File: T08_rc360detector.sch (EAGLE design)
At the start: 46 parts, among them IC2 LM317MSTT3, U1 ATmega328, X1 SSW-101-02-S-D, X2 332-04, X4 87758-0616, X5 87758-0616

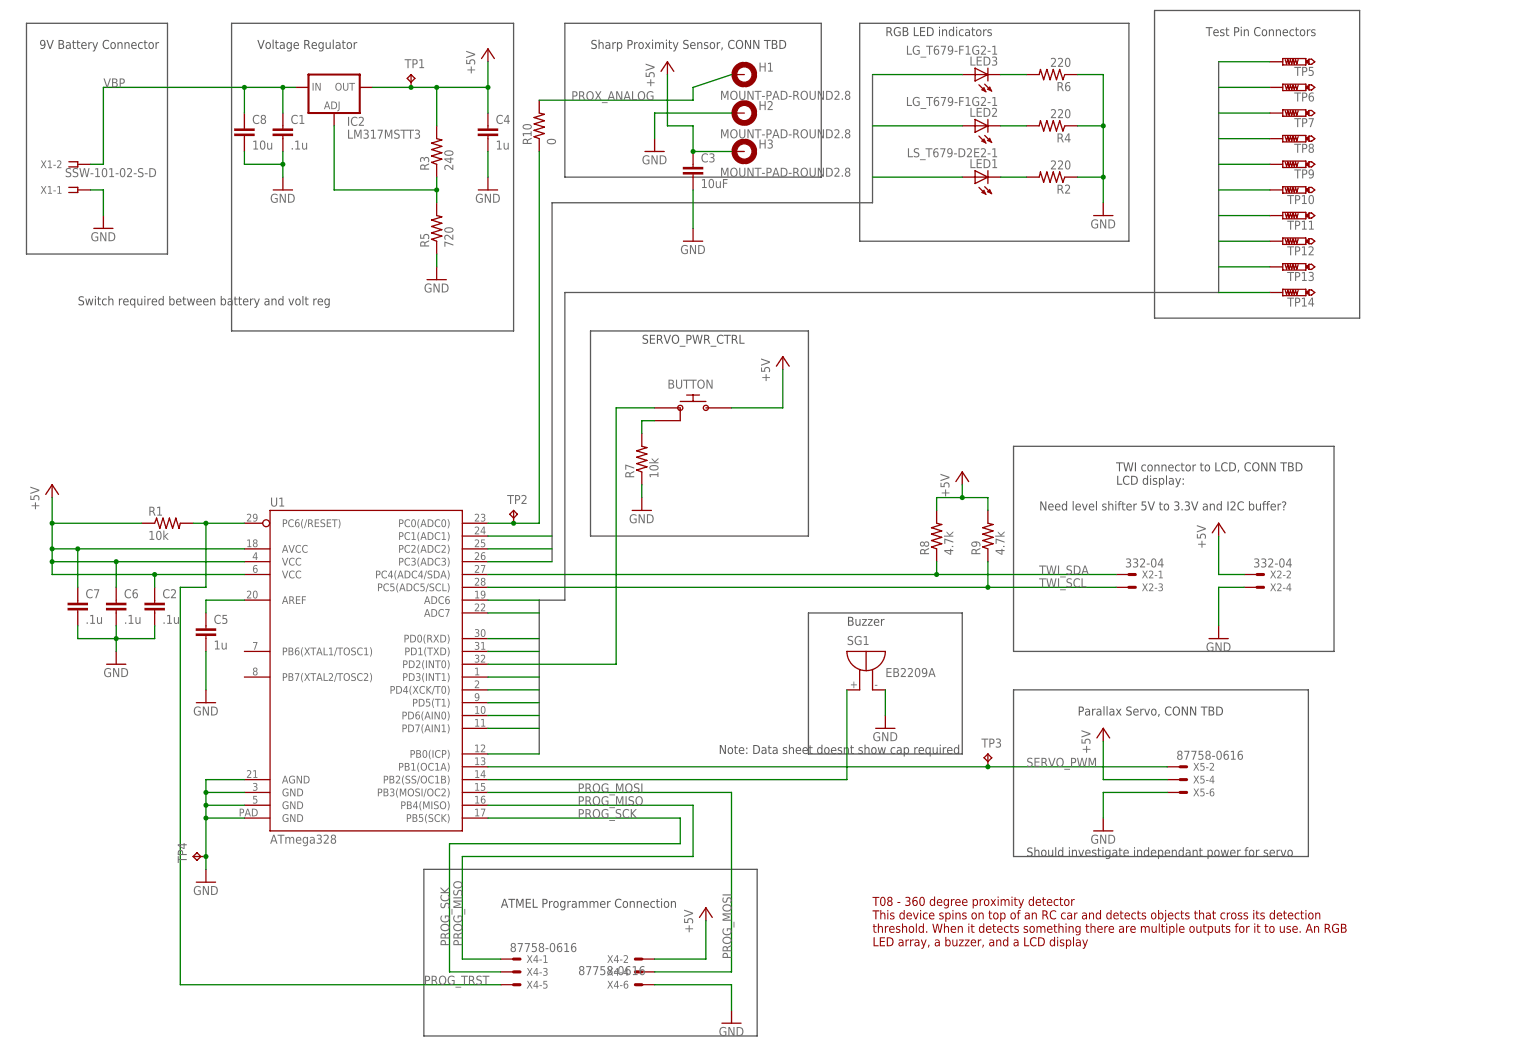
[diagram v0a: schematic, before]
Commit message: First pass at board layout
Started board layout. The problems:
-The current atmega328 block is way too small for us to solder, changed
to the pdip for the moment
-not sure if I got the rules check file working
-PCB layers are at 16, and it should be 2
-Need mounting screws tied to ground added to sch
-Added second power supply for servo
-Need to change layout to buzzer I found. Dimensions in components wiki
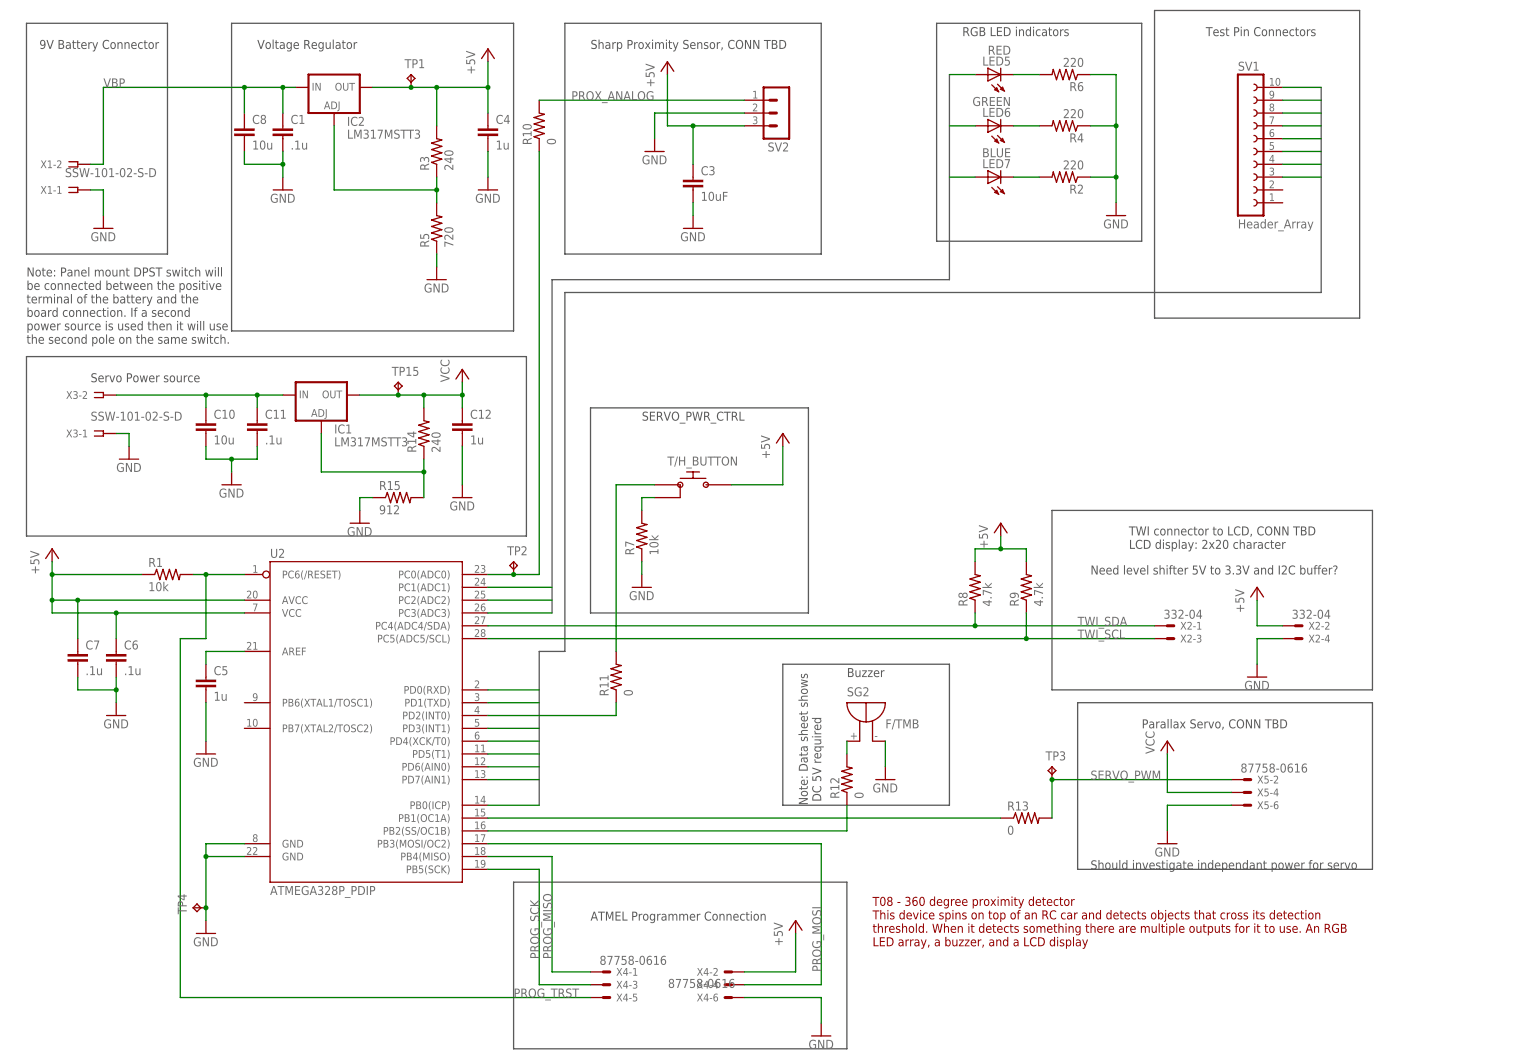
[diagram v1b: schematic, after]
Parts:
- removed BUTTON: PR141C, 360prox:PR141C
- removed C2: .1u, rcl:C-EUC0805
- removed H1, H2, H3: MOUNT-PAD-ROUND2.8, holes:MOUNT-PAD-ROUND2.8
- removed LED1: LS_T679-D2E2-1, led:LS_T679-D2E2-1
- removed LED2, LED3: LG_T679-F1G2-1, led:LG_T679-F1G2-1
- removed SG1: EB2209A, buzzer:EB2209A
- removed TP10, TP11, TP12, TP13, TP14, TP5, TP6, TP7, TP8, TP9: PTR1PAD1-20, testpad:PTR1PAD1-20
- removed U1: ATmega328, SparkFun-DigitalIC:ATMEGA328P_MLFMLF32
- added C10: 10u, rcl:C-EUC0805
- added C11: .1u, resistor:C-EUC0805
- added C12: 1u, resistor:C-EUC0805
- added IC1: LM317MSTT3, v-reg:LM317MSTT3
- added LED5: RED, led:LEDLD260
- added LED6: GREEN, led:LEDLD260
- added LED7: BLUE, led:LEDLD260
- added R11, R12, R13: 0, rcl:R-US_R0805
- added R14: 240, rcl:R-US_R0805
- added R15: 912, rcl:R-US_R0805
- added SG2: F/TMB, buzzer:F/TMB
- added SV1: Header_Array, con-lsta:FE10-1
- added SV2: (no value), con-lstb:MA03-1
- added T/H_BUTTON: PR141C, 360prox:PR141C
- added TP15: TPTP15R, testpad:TPTP15R
- added U2: ATMEGA328P_PDIP, SparkFun-DigitalIC:ATMEGA328P_PDIP
- added X3: SSW-101-02-S-D, con-samtec:SSW-101-02-S-D
- C1, C4, C5: device rcl:C-EUC0603 -> resistor:C-EUC0805
- R1, R3, R5: device rcl:R-US_R0603 -> rcl:R-US_R0805
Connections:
- removed net TP0: TP5.TP, U1.ADC6
- removed net TP1: TP6.TP, U1.ADC7
- new net N$10: R12.1, U2.PB2(SS/OC1B)
- new net N$11: R13.1, U2.PB1(OC1A)
- new net N$13: IC1.ADJ, R14.1, R15.2
- new net N$14: C10.1, C11.1, IC1.IN, X3-2.1
- new net N$6: R11.2, T/H_BUTTON.IN
- new net VCC: C12.1, IC1.OUT, R14.2, TP15.TP, X5-4.S
- net +5V: now also SV2.3, T/H_BUTTON.OUT, U2.AVCC, U2.VCC; no longer BUTTON.OUT, C2.1, H3.MOUNT, U1.AVCC, U1.VCC@4, U1.VCC@6, X5-4.S
- net AREF: now also U2.AREF; no longer U1.AREF
- net GND: now also C10.2, C11.2, C12.2, R15.1, SG2.-, SV2.2, U2.GND@1, U2.GND@2, X3-1.1; no longer C2.2, H2.MOUNT, SG1.-, U1.AGND, U1.GND@3, U1.GND@5, U1.GND@PAD
- net LED0: now also LED5.A, U2.PC1(ADC1); no longer LED1.A, U1.PC1(ADC1)
- net LED1: now also LED6.A, U2.PC2(ADC2); no longer LED2.A, U1.PC2(ADC2)
- net LED2: now also LED7.A, U2.PC3(ADC3); no longer LED3.A, U1.PC3(ADC3)
- net N$1: now also T/H_BUTTON.GND; no longer BUTTON.GND
- net N$3: now also R11.1, U2.PD2(INT0); no longer BUTTON.IN, U1.PD2(INT0)
- net N$4: now also R12.2, SG2.+; no longer SG1.+, U1.PB2(SS/OC1B)
- net N$5: now also LED5.C; no longer LED3.C
- net N$7: now also LED6.C; no longer LED2.C
- net N$8: now also LED7.C; no longer LED1.C
- net N$9: now also U2.PC0(ADC0); no longer U1.PC0(ADC0)
- net PROG_MISO: now also U2.PB4(MISO); no longer U1.PB4(MISO)
- net PROG_MOSI: now also U2.PB3(MOSI/OC2); no longer U1.PB3(MOSI/OC2)
- net PROG_SCK: now also U2.PB5(SCK); no longer U1.PB5(SCK)
- net PROG_TRST: now also U2.PC6(/RESET); no longer U1.PC6(/RESET)
- net PROX_ANALOG: now also SV2.1; no longer H1.MOUNT
- net SERVO_PWM: now also R13.2; no longer U1.PB1(OC1A)
- net TP2: now also SV1.3, U2.PD0(RXD); no longer TP7.TP, U1.PD0(RXD)
- net TP3: now also SV1.4, U2.PD1(TXD); no longer TP8.TP, U1.PD1(TXD)
- net TP4: now also SV1.5, U2.PD3(INT1); no longer TP9.TP, U1.PD3(INT1)
- net TP5: now also SV1.6, U2.PD4(XCK/T0); no longer TP10.TP, U1.PD4(XCK/T0)
- net TP6: now also SV1.7, U2.PD5(T1); no longer TP11.TP, U1.PD5(T1)
- net TP7: now also SV1.8, U2.PD6(AIN0); no longer TP12.TP, U1.PD6(AIN0)
- net TP8: now also SV1.9, U2.PD7(AIN1); no longer TP13.TP, U1.PD7(AIN1)
- net TP9: now also SV1.10, U2.PB0(ICP); no longer TP14.TP, U1.PB0(ICP)
- net TWI_SCL: now also U2.PC5(ADC5/SCL); no longer U1.PC5(ADC5/SCL)
- net TWI_SDA: now also U2.PC4(ADC4/SDA); no longer U1.PC4(ADC4/SDA)
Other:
- note added: "Note: Data sheet shows DC 5V required"
- note added: "Note: Panel mount DPST switch will be connected between the positive terminal of the battery and the board connection. If a second power source is used then it will use the second pole on the same switch."
- note added: "Servo Power source"
- note added: "TWI connector to LCD, CONN TBD LCD display: 2x20 character"
- note removed: "Note: Data sheet doesnt show cap required"
- note removed: "Switch required between battery and volt reg"
- note removed: "TWI connector to LCD, CONN TBD LCD display:"
- moved on the sheet: C3, C5, C6, C7, R1, R2, R4, R6, R7, R8, R9, TP2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

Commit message: 2nd pass
-Added custom library that contains button and buzzer
-Routed rest of connections. Left TWI interface out until Jared adds the
finished connections to the schematic
-Added screw holes, can resize if we want bigger screws
-Added some basic silk screen
-Added jumper for servo so we can switch it between if needed.
-Still need to find actual LEDs, until then there are generic T/H
-Havnt touched DRC, must look into in future
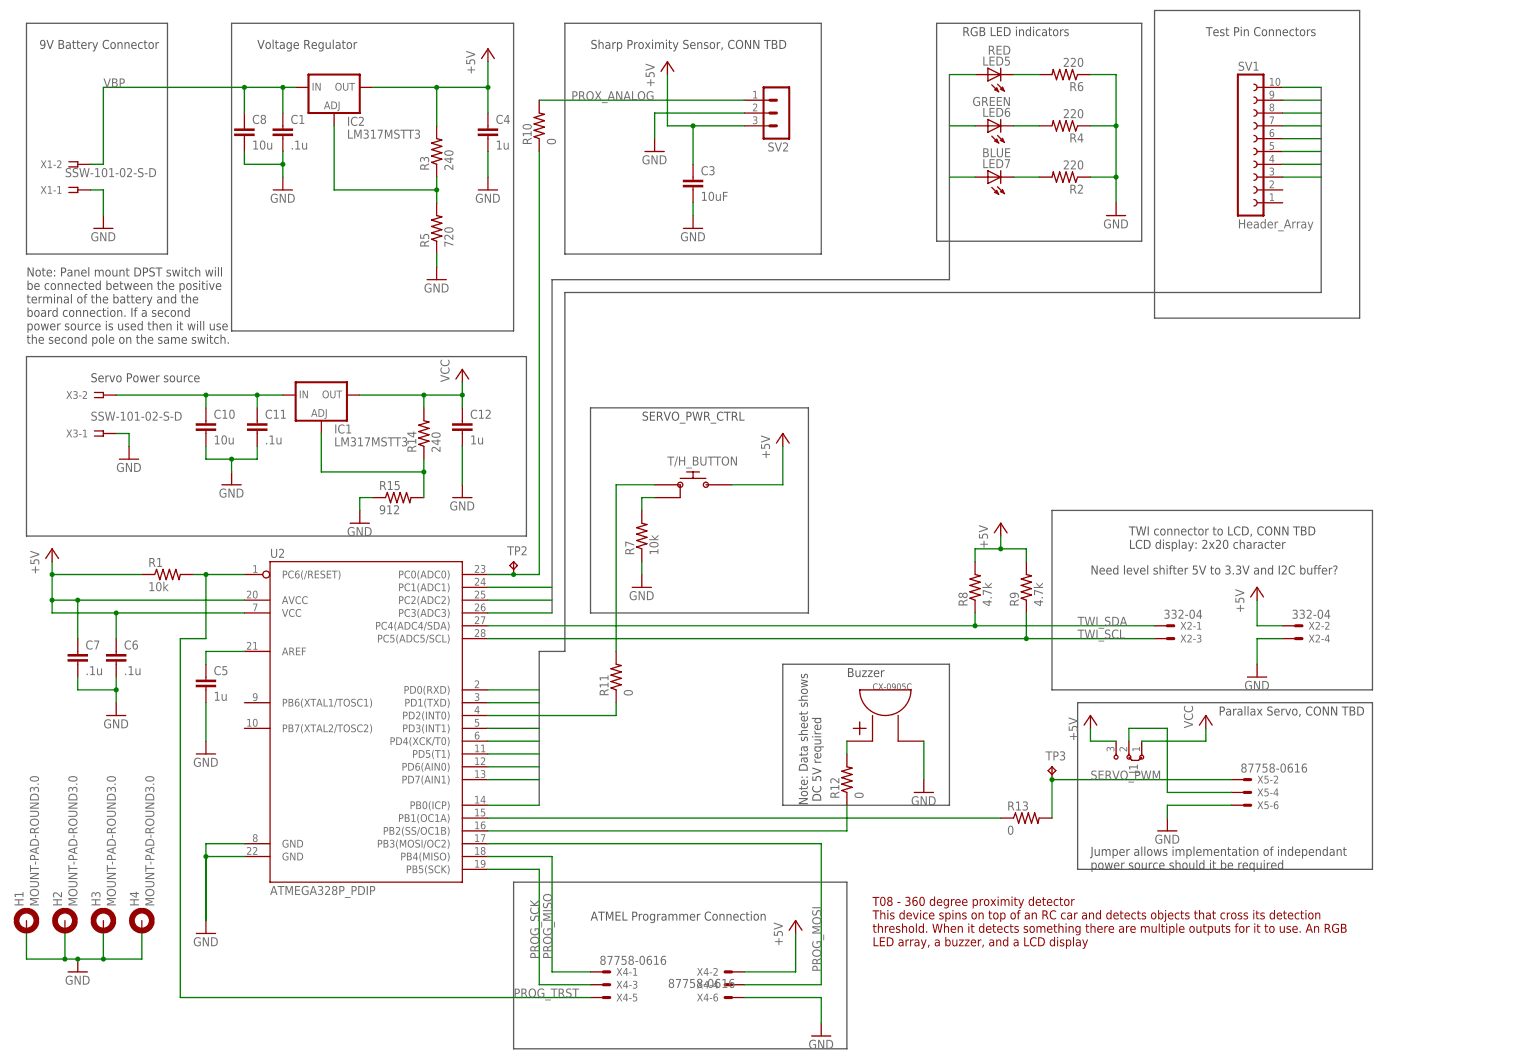
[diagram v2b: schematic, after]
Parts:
- removed SG2: F/TMB, buzzer:F/TMB
- removed TP1, TP4: TPPAD1-17, testpad:TPPAD1-17
- removed TP15: TPTP15R, testpad:TPTP15R
- added CX-0905C: CX-0905C, 360prox:CX-0905C
- added H1, H2, H3, H4: MOUNT-PAD-ROUND3.0, holes:MOUNT-PAD-ROUND3.0
- added J1: (no value), jumper:J2X2MM
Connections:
- new net N$16: J1.2, X5-4.S
- net +5V: now also J1.3; no longer TP1.TP
- net GND: now also CX-0905C.OUT, H1.MOUNT, H2.MOUNT, H3.MOUNT, H4.MOUNT; no longer SG2.-, TP4.TP
- net N$4: now also CX-0905C.IN; no longer SG2.+
- net VCC: now also J1.1; no longer TP15.TP, X5-4.S
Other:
- note added: "Jumper allows implementation of independant power source should it be required"
- note removed: "Should investigate independant power for servo"

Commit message: Update
Rerouted layout with new TWI circuitry. The logic converter IC is so
small the chip doesnt pass DRC, so I informed Jared and he's looking
into an alternate solution. Also the current chip is PDIP but I'm
debating changing it to TQFP. Will need to discuss tomorrow.
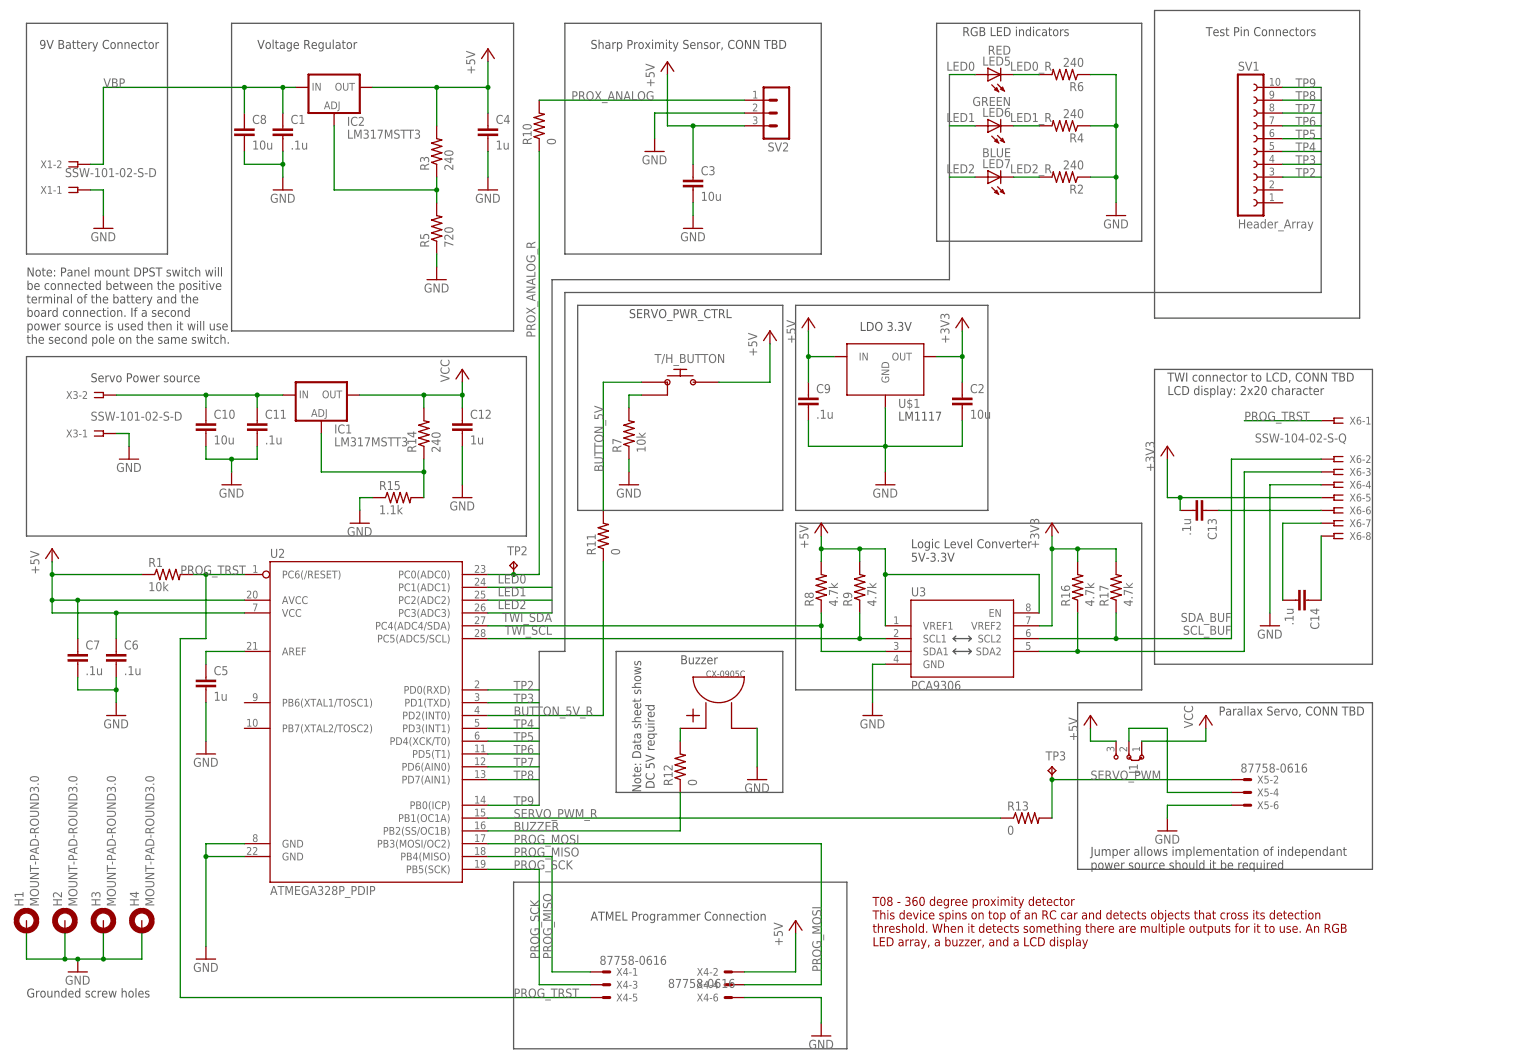
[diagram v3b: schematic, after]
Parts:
- removed X2: 332-04, con-garry:332-04
- added C13, C14, C9: .1u, resistor:C-EUC0805
- added C2: 10u, rcl:C-EUC0805
- added R16, R17: 4.7k, rcl:R-US_R0805
- added U$1: LM1117, 360prox:LM1117
- added U3: PCA9306, SparkFun-DigitalIC:PCA9306
- added X6: SSW-104-02-S-Q, con-samtec:SSW-104-02-S-Q
- C3: value 10uF -> 10u
- R15: value 912 -> 1.1k
- R2, R4, R6: value 220 -> 240
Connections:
- net N$10 renamed BUZZER
- net N$11 renamed SERVO_PWM_R
- net N$3 renamed BUTTON_5V_R
- net N$5 renamed LED0_R
- net N$6 renamed BUTTON_5V
- net N$7 renamed LED1_R
- net N$8 renamed LED2_R
- net N$9 renamed PROX_ANALOG_R
- new net +3V3: C13.2, C2.1, R16.2, R17.2, U$1.OUT, U3.VREF2, X6-5.1
- new net N$18: C13.1, X6-6.1
- new net N$19: C14.2, X6-7.1
- new net N$20: C14.1, X6-8.1
- new net SCL_BUF: R17.1, U3.SCL2, X6-2.1
- new net SDA_BUF: R16.1, U3.SDA2, X6-3.1
- net +5V: now also C9.1, U$1.IN, U3.EN, U3.VREF1; no longer X2-2.S
- net GND: now also C2.2, C9.2, U$1.GND, U3.GND, X6-4.1; no longer X2-4.S
- net PROG_TRST: now also X6-1.1
- net TWI_SCL: now also U3.SCL1; no longer X2-3.S
- net TWI_SDA: now also U3.SDA1; no longer X2-1.S
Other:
- note added: "Grounded screw holes"
- note added: "LDO 3.3V"
- note added: "Logic Level Converter 5V-3.3V"
- note removed: "Need level shifter 5V to 3.3V and I2C buffer?"
- moved on the sheet: CX-0905C, R11, R12, R7, R8, R9, T/H_BUTTON
